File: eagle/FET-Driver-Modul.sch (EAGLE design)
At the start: 19 parts, among them X1 MKDSN1,5/3-5,08

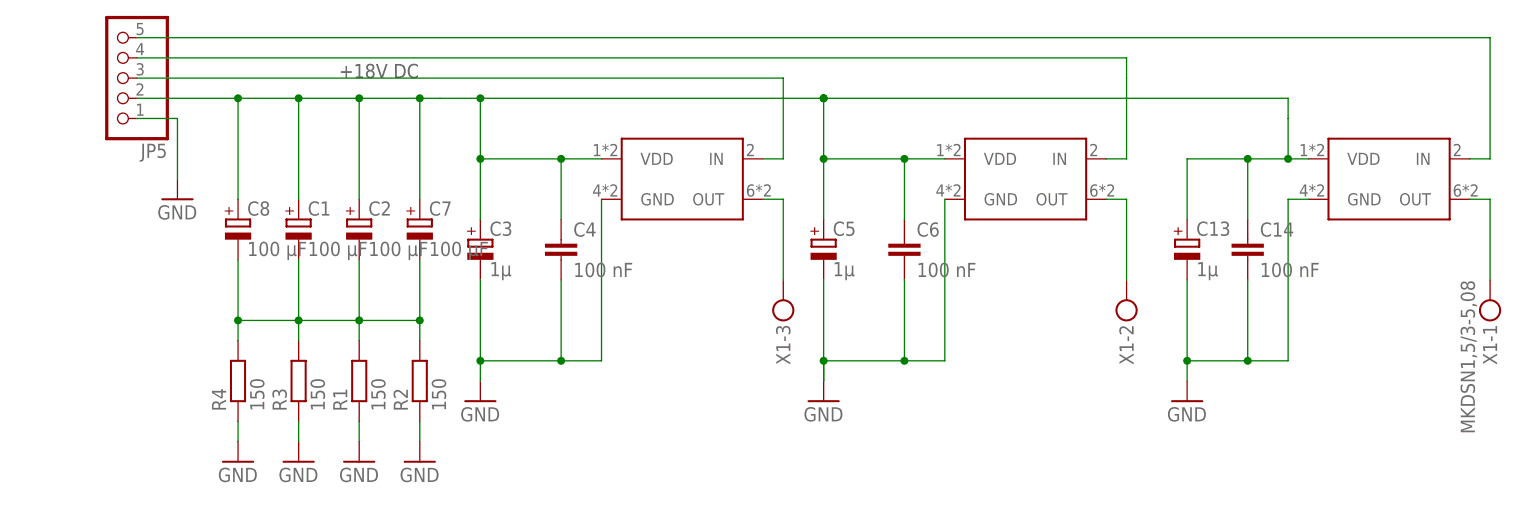
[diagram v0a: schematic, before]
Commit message: Minor documentation changes, reduced size of vsens Resistor to detect contact
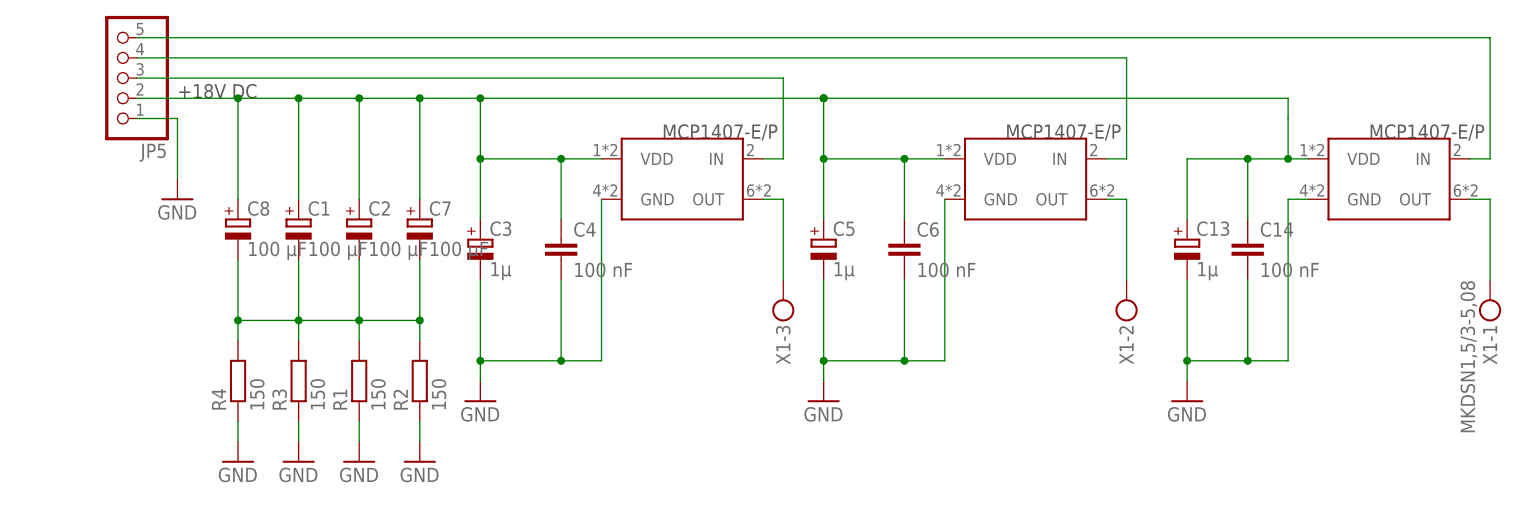
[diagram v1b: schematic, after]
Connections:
- removed net GND1: C5.-, C6.2, U$4.GND
- net GND: now also C5.-, C6.2, U$4.GND
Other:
- note added: "MCP1407-E/P"
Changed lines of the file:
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@@
 <sheet>
 <plain>
-<text x="0" y="17.78" size="1.778" layer="97">+18V DC</text>
+<text x="-20.32" y="15.24" size="1.778" layer="97">+18V DC</text>
+<text x="40.64" y="10.16" size="1.778" layer="97">MCP1407-E/P</text>
+<text x="83.82" y="10.16" size="1.778" layer="97">MCP1407-E/P</text>
+<text x="129.54" y="10.16" size="1.778" layer="97">MCP1407-E/P</text>
 </plain>
 <instances>
@@
 </segment>
 <segment>
-<pinref part="GND29" gate="1" pin="GND"/>
-<wire x1="60.96" y1="-20.32" x2="60.96" y2="-17.78" width="0.1524" layer="91"/>
-</segment>
-<segment>
 <pinref part="U$5" gate="G$1" pin="GND"/>
 <wire x1="121.92" y1="2.54" x2="119.38" y2="2.54" width="0.1524" layer="91"/>
@@
 <wire x1="10.16" y1="-25.4" x2="10.16" y2="-27.94" width="0.1524" layer="91"/>
 </segment>
+<segment>
+<wire x1="60.96" y1="-17.78" x2="71.12" y2="-17.78" width="0.1524" layer="91"/>
+<pinref part="C5" gate="G$1" pin="-"/>
+<wire x1="60.96" y1="-7.62" x2="60.96" y2="-17.78" width="0.1524" layer="91"/>
+<pinref part="C6" gate="G$1" pin="2"/>
+<wire x1="71.12" y1="-7.62" x2="71.12" y2="-17.78" width="0.1524" layer="91"/>
+<pinref part="U$4" gate="G$1" pin="GND"/>
+<wire x1="76.2" y1="2.54" x2="76.2" y2="-17.78" width="0.1524" layer="91"/>
+<wire x1="76.2" y1="-17.78" x2="71.12" y2="-17.78" width="0.1524" layer="91"/>
+<junction x="71.12" y="-17.78"/>
+<pinref part="GND29" gate="1" pin="GND"/>
+<wire x1="60.96" y1="-17.78" x2="60.96" y2="-20.32" width="0.1524" layer="91"/>
+<junction x="60.96" y="-17.78"/>
+</segment>
 </net>
 <net name="N$33" class="0">
@@
 </segment>
 </net>
-<net name="GND1" class="0">
-<segment>
-<wire x1="60.96" y1="-20.32" x2="60.96" y2="-17.78" width="0.1524" layer="91"/>
-<wire x1="60.96" y1="-17.78" x2="71.12" y2="-17.78" width="0.1524" layer="91"/>
-<pinref part="C5" gate="G$1" pin="-"/>
-<wire x1="60.96" y1="-7.62" x2="60.96" y2="-17.78" width="0.1524" layer="91"/>
-<junction x="60.96" y="-17.78"/>
-<pinref part="C6" gate="G$1" pin="2"/>
-<wire x1="71.12" y1="-7.62" x2="71.12" y2="-17.78" width="0.1524" layer="91"/>
-<pinref part="U$4" gate="G$1" pin="GND"/>
-<wire x1="76.2" y1="2.54" x2="76.2" y2="-17.78" width="0.1524" layer="91"/>
-<wire x1="76.2" y1="-17.78" x2="71.12" y2="-17.78" width="0.1524" layer="91"/>
-<junction x="71.12" y="-17.78"/>
-</segment>
-</net>

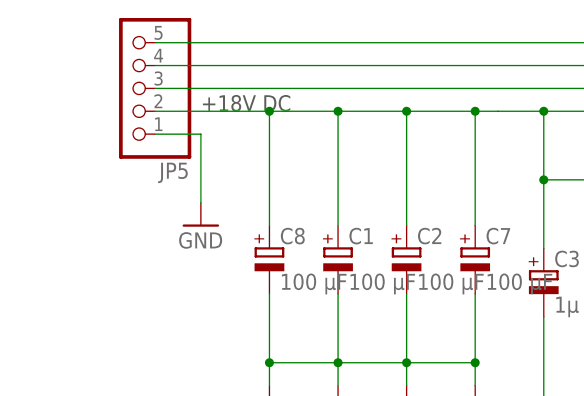
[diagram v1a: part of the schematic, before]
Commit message: additional diode at Mosfet driver
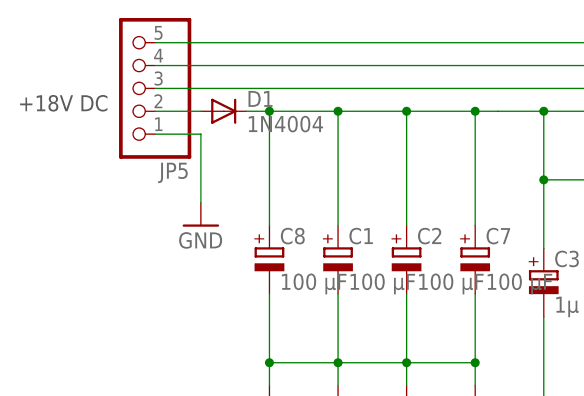
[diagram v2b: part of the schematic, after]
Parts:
- added D1: 1N4004, diode:1N4004
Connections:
- new net N$6: D1.A, JP5.2
- net N$2: now also D1.C; no longer JP5.2
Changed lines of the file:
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@@
 <part name="GND4" library="supply1" deviceset="GND" device=""/>
 <part name="GND5" library="supply1" deviceset="GND" device=""/>
+<part name="D1" library="diode" deviceset="1N4004" device=""/>
 </parts>
 <sheets>
 <sheet>
 <plain>
-<text x="-20.32" y="15.24" size="1.778" layer="97">+18V DC</text>
+<text x="-40.64" y="15.24" size="1.778" layer="97">+18V DC</text>
 <text x="40.64" y="10.16" size="1.778" layer="97">MCP1407-E/P</text>
 <text x="83.82" y="10.16" size="1.778" layer="97">MCP1407-E/P</text>
@@
 <instance part="GND4" gate="1" x="-12.7" y="-30.48"/>
 <instance part="GND5" gate="1" x="10.16" y="-30.48"/>
+<instance part="D1" gate="1" x="-17.78" y="15.24"/>
 </instances>
 <busses>
@@
 <junction x="60.96" y="15.24"/>
 <junction x="60.96" y="15.24"/>
-<pinref part="JP5" gate="A" pin="2"/>
-<wire x1="-25.4" y1="15.24" x2="-12.7" y2="15.24" width="0.1524" layer="91"/>
 <pinref part="C1" gate="G$1" pin="+"/>
+<wire x1="-15.24" y1="15.24" x2="-12.7" y2="15.24" width="0.1524" layer="91"/>
 <wire x1="-12.7" y1="15.24" x2="-5.08" y2="15.24" width="0.1524" layer="91"/>
 <wire x1="-5.08" y1="15.24" x2="2.54" y2="15.24" width="0.1524" layer="91"/>
@@
 <wire x1="-12.7" y1="15.24" x2="-12.7" y2="2.54" width="0.1524" layer="91"/>
 <junction x="-12.7" y="15.24"/>
+<pinref part="D1" gate="1" pin="C"/>
 </segment>
 </net>
@@
 </segment>
 </net>
+<net name="N$6" class="0">
+<segment>
+<pinref part="JP5" gate="A" pin="2"/>
+<wire x1="-25.4" y1="15.24" x2="-20.32" y2="15.24" width="0.1524" layer="91"/>
+<pinref part="D1" gate="1" pin="A"/>
+</segment>
+</net>
